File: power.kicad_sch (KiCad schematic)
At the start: 24 parts, among them Q1 DMN3008SFG, Q2 DMN3008SFG, U1 AP33771, U2 AP62150WU

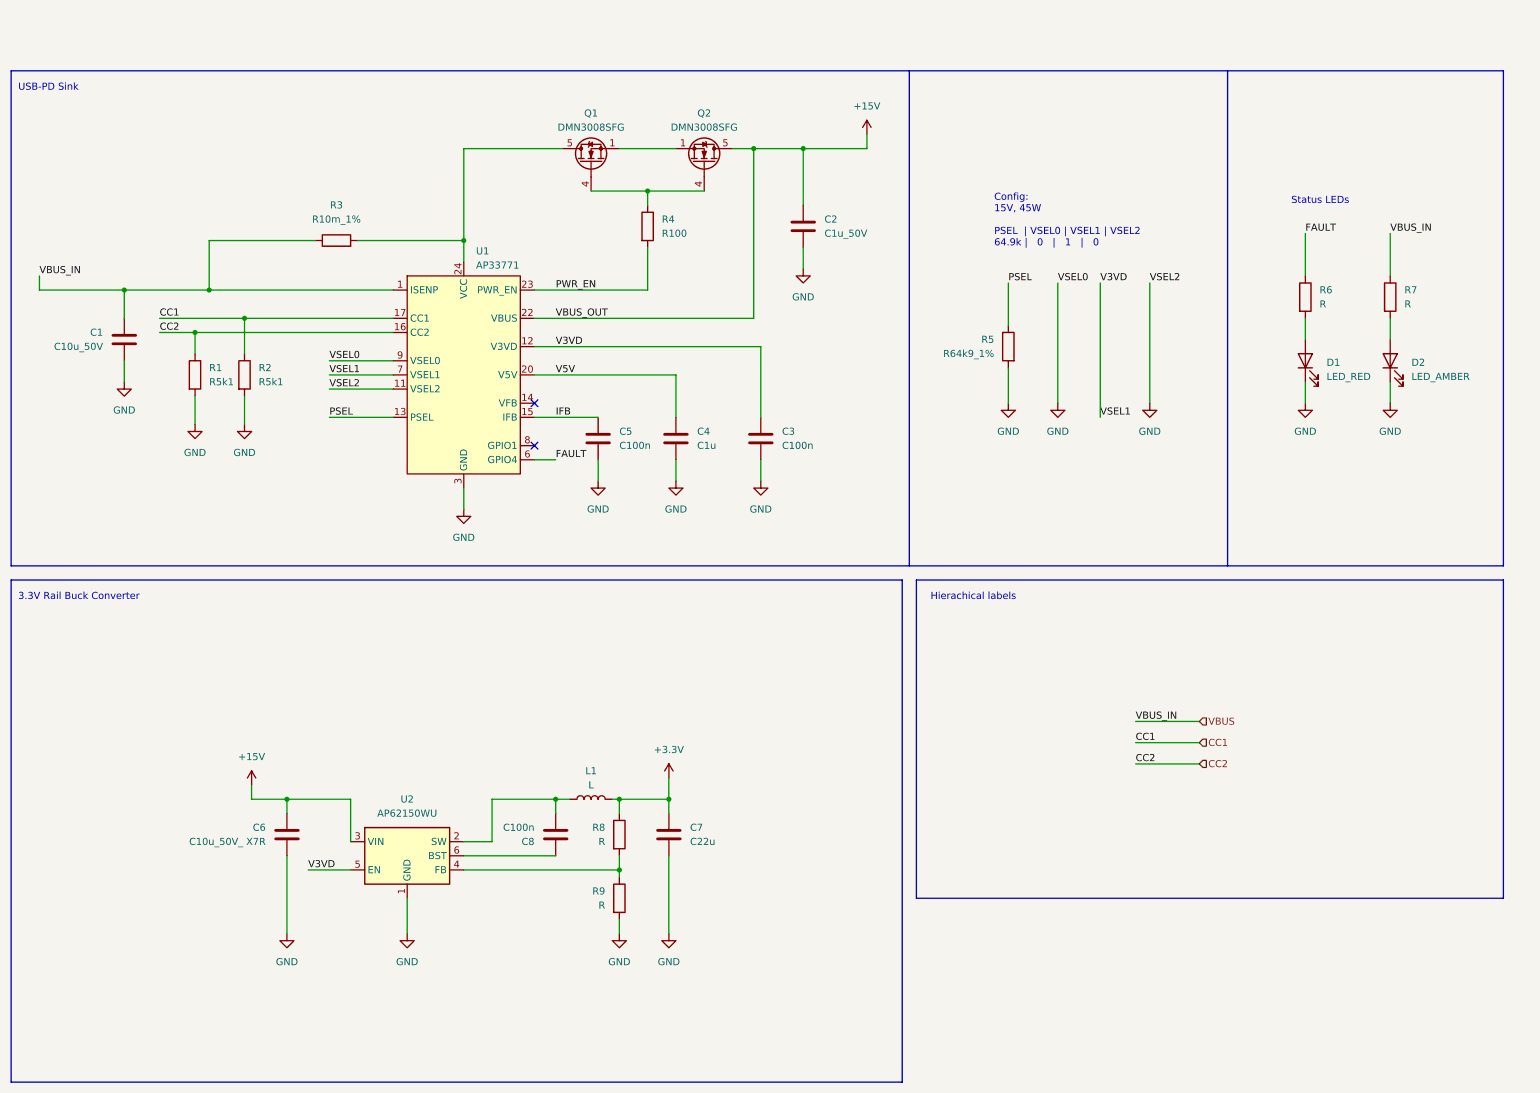
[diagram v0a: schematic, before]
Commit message: Add ESP32-S3-WROOM-1, 5V rail and UI sheet
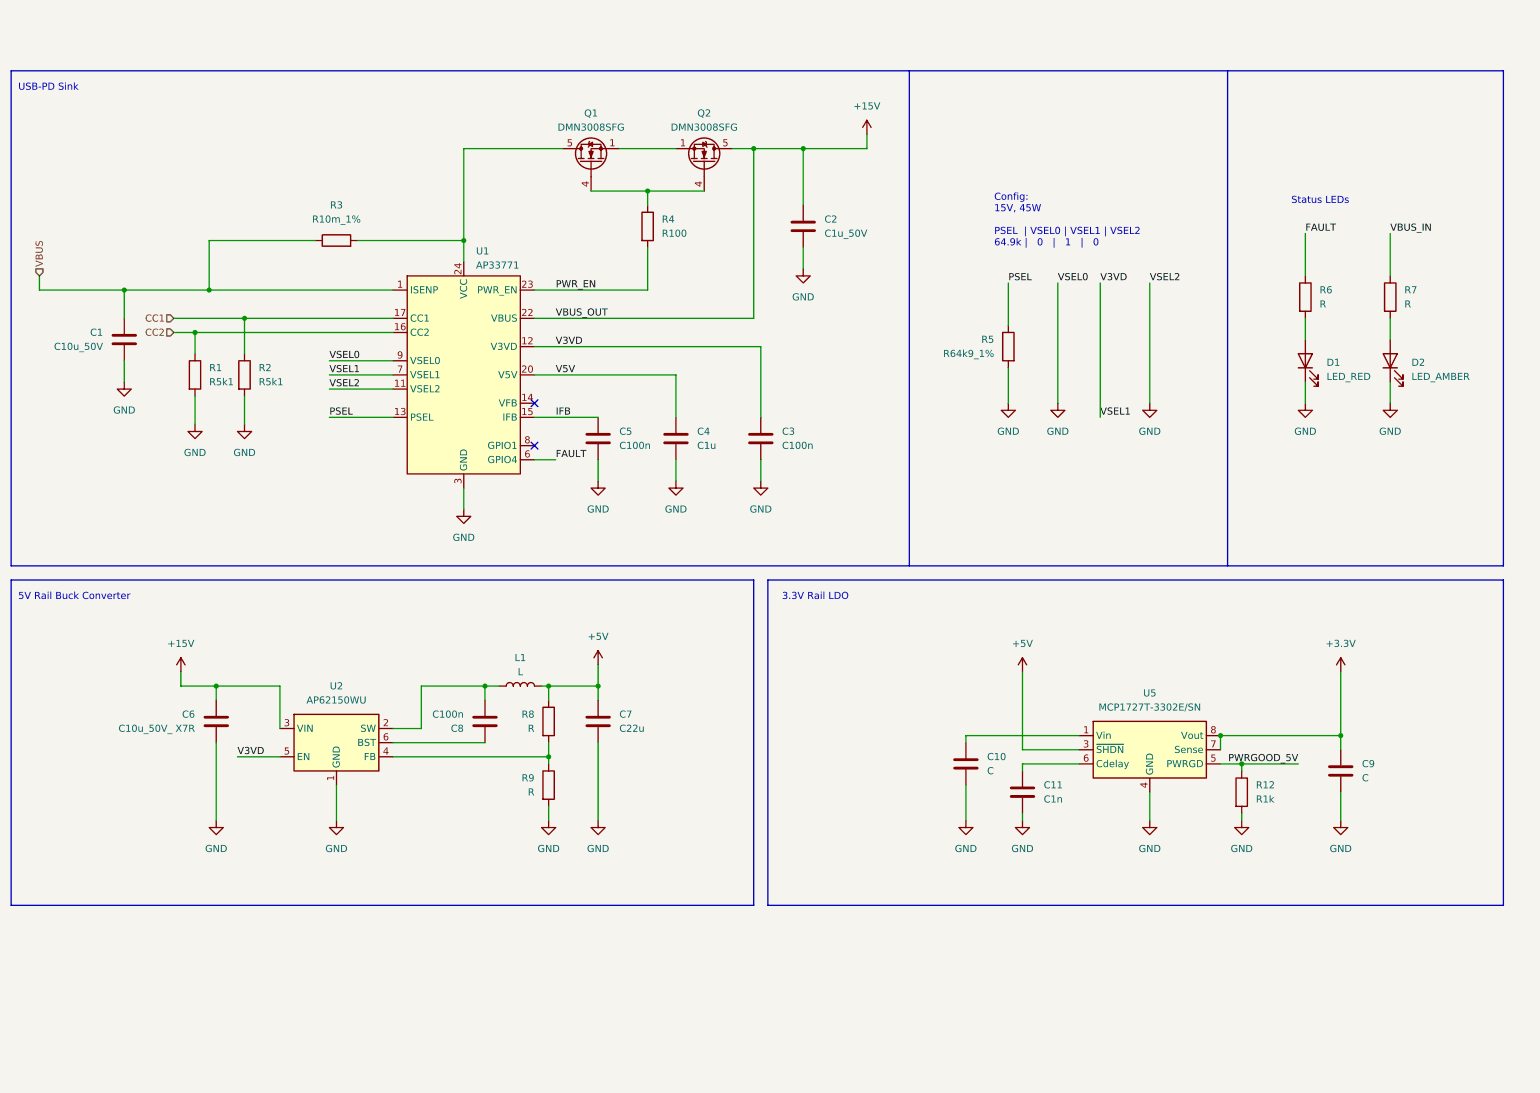
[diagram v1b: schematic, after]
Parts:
- added C10, C9: C, symbol Device:C
- added C11: C1n, symbol Device:C
- added R12: R1k, symbol Device:R
- added U5: MCP1727T-3302E/SN, Package_SO:SOIC-8_3.9x4.9mm_P1.27mm, symbol Regulator_Linear:MCP1727-3302xSN
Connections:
- net +3.3V: now also C9.1, U5.7 (Sense), U5.8 (Vout); no longer C7.1, L1.2, R8.1
- net GND: now also C10.2, C11.2, C9.2, R12.2, U5.4 (GND)
- net VBUS: no longer R7.1
- new net: C10.1, U5.1 (Vin), U5.2 (Vin)
- new net: C11.1, U5.6 (Cdelay)
- new net +5V: C7.1, L1.2, R8.1, U5.3 (~{SHDN})
- new net PWRGOOD_5V: R12.1, U5.5 (PWRGD)
- new net VBUS_IN: R7.1
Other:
- note added: "3.3V Rail LDO"
- note added: "5V Rail Buck Converter"
- note removed: "3.3V Rail Buck Converter"
- note removed: "Hierachical labels"
- moved on the sheet: C6, C7, C8, L1, R8, R9, U2

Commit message: Finish first design
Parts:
- removed R12: R1k, symbol Device:R
- removed U5: MCP1727T-3302E/SN, Package_SO:SOIC-8_3.9x4.9mm_P1.27mm, symbol Regulator_Linear:MCP1727-3302xSN
- added C20: C100u_20V, Capacitor_SMD:CP_Elec_6.3x5.9, symbol Device:C_Polarized
- added L2: L3u3, Inductor_SMD:L_Coilcraft_LPS4018, symbol Device:L
- added R29: R31k6_1%, Resistor_SMD:R_0805_2012Metric, symbol Device:R
- added R31: R10k_1%, Resistor_SMD:R_0805_2012Metric, symbol Device:R
- added TP18, TP19, TP20, TP21, TP22, TP25, TP26: TestPoint_Small, TestPoint:TestPoint_Pad_D1.5mm, symbol Connector:TestPoint_Small
- added U4: AP62150WU, Package_TO_SOT_SMD:TSOT-23-6, symbol Regulator_Switching:AP62150WU
- added U5: USBLC6-2SC6, Package_TO_SOT_SMD:SOT-23-6, symbol Power_Protection:USBLC6-2SC6
- C1: value C10u_50V -> C10u_25V; footprint (none) -> Capacitor_SMD:C_0603_1608Metric; Mouser Part Number (none) -> 81-GRM188R61E106KA3J
- C10: value C -> C100n; footprint (none) -> Capacitor_SMD:C_0603_1608Metric; Mouser Part Number (none) -> 80-C0603C104K3R7867
- C11: value C1n -> C22u; footprint (none) -> Capacitor_SMD:C_0805_2012Metric; Mouser Part Number (none) -> 187-CL21A226MQQNNNF
- C2: value C1u_50V -> C1u_25V; footprint (none) -> Capacitor_SMD:C_0603_1608Metric; Mouser Part Number (none) -> 963-TMK107B7105MA-T
- C3, C5, C8: footprint (none) -> Capacitor_SMD:C_0603_1608Metric; Mouser Part Number (none) -> 80-C0603C104K3R7867
- C4: value C1u -> C1u_25V; footprint (none) -> Capacitor_SMD:C_0603_1608Metric; Mouser Part Number (none) -> 963-TMK107B7105MA-T
- C6: value C10u_50V_ X7R -> C10u_25V; footprint (none) -> Capacitor_SMD:C_0603_1608Metric; Mouser Part Number (none) -> 81-GRM188R61E106KA3J
- C7: footprint (none) -> Capacitor_SMD:C_0805_2012Metric; Mouser Part Number (none) -> 187-CL21A226MQQNNNF
- C9: value C -> C10u_25V; footprint (none) -> Capacitor_SMD:C_0603_1608Metric; Mouser Part Number (none) -> 81-GRM188R61E106KA3J
- D1: value LED_RED -> LTST-C230CKT; footprint (none) -> project:LTST-C230; Mouser Part Number (none) -> 859-LTST-C230CKT
- D2: value LED_AMBER -> LTST-C230KGKT; footprint (none) -> project:LTST-C230; Mouser Part Number (none) -> 859-LTST-C230KGKT
- L1: value L -> L3u3; footprint (none) -> Inductor_SMD:L_Coilcraft_LPS4018; Mouser Part Number (none) -> 994-LPS4018-332MRC
- Q1, Q2: Mouser Part Number (none) -> 621-DMN3008SFG-7
- R1, R2: footprint (none) -> Resistor_SMD:R_0603_1608Metric; Mouser Part Number (none) -> 667-ERJ-3EKF5101V
- R3: value R10m_1% -> R10m_1%_0.5W; footprint (none) -> Resistor_SMD:R_1206_3216Metric; Mouser Part Number (none) -> 504-MFL1206R0100FS
- R4: footprint (none) -> Resistor_SMD:R_0603_1608Metric; Mouser Part Number (none) -> 279-CRG0603F100R
- R5: footprint (none) -> Resistor_SMD:R_0603_1608Metric; Mouser Part Number (none) -> 603-RC0603FR-0764K9P
- R6: value R -> R300; footprint (none) -> Resistor_SMD:R_0805_2012Metric; Mouser Part Number (none) -> 791-WR08X3000FTL
- R7: value R -> R2k7; footprint (none) -> Resistor_SMD:R_0805_2012Metric; Mouser Part Number (none) -> 279-CRGCQ0805F2K7
- R8: value R -> R52k3_1%; footprint (none) -> Resistor_SMD:R_0805_2012Metric; Mouser Part Number (none) -> 652-CR0805FX-5232ELF
- R9: value R -> R10k_1%; footprint (none) -> Resistor_SMD:R_0805_2012Metric; Mouser Part Number (none) -> 71-CRCW0805-10K-E3
- U1: Mouser Part Number (none) -> 621-AP33771DKZ-13
- U2: Mouser Part Number (none) -> 621-AP62150WU-7
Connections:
- net VBUS_IN is gone; now on net +15V: R7.1
- net +15V: now also C20.1, TP20.1
- net +3.3V: now also C11.1, U2.5 (EN), L2.2, R29.1, TP26.1; no longer C9.1
- net +5V: now also TP25.1
- net GND: now also C20.2, R31.2, U4.1 (GND), U5.2 (GND); no longer C10.2
- net V3VD: now also TP21.1, U4.5 (EN); no longer U2.5 (EN)
- net V5V: now also TP22.1, U5.5 (VBUS)
- net VBUS: now also TP18.1
- net 5V_BUCK_SW: now reaches C8.1, L1.1, U2.2 (SW)
- net 5V_BUCK_FB: now reaches R8.2, R9.1, U2.4 (FB)
- net PWR_EN_GATE: now reaches Q1.4 (G), Q2.4 (G), R4.1
- net 3V3_BUCK_SW: now reaches C10.1
- net 3V3_BUCK_SW: now also L2.1, U4.2 (SW)
- net 5V_BUCK_BST: now reaches C8.2, U2.6 (BST)
- net PWR_SOURCE_DRAIN: now reaches Q1.1 (S), Q1.2 (S), Q1.3 (S), Q2.1 (S), Q2.2 (S), Q2.3 (S)
- net PWR_VCC: now reaches Q1.5 (D), R3.2, U1.24 (VCC)
- net PWR_VCC: now also C9.1, TP19.1, U4.3 (VIN)
- net FAULT renamed PWR_FAULT
- new net 3V3_BUCK_BST: C10.2, U4.6 (BST)
- new net 3V3_BUCK_FB: R29.2, R31.1, U4.4 (FB)
- new net USB_D+: U5.1 (I/O1), U5.6 (I/O1)
- new net USB_D-: U5.3 (I/O2), U5.4 (I/O2)
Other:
- note added: "15V USB-PD Sink (60W/4A) supply for: - Valves - Main / Aux. Pump & Driver - 5V Buck Converter Decided to use 15V for Pumps and Valves, since the PD-Sink can't negotiate 12V. Also adding another 12V rail would raise the cost and complexity. Did some tests with the Pumps and Valves, they get a bit hotter than with 12V but since they are not driven too long this should not be a Problem."
- note added: "3.3V Rail Buck(4.95W/1.5A) supply for: - MCU - Display used recommended values from datasheet page 15, table 1"
- note added: "5V Rail Buck Converter (7.5W/1.5A) supply for: - Servo - HX711 used recommended values from datasheet page 15, table 1"
- note added: "Check: Find cheaper replacement"
- note added: "Config: 15V, | 60W | 15V | | PSEL | VSEL0 | VSEL1 | VSEL2 | | 75k | 0 | 1 | 0 | see datasheet page 2"
- note added: "MCU should be able to also run before 15V can be supplied reliably!! PWR_VCC can be either 5V or 15V"
- note added: "Shunt power rating: Voltage drop: 4A * 0.01R = 0.04V Power dissipation: 0.04V * 4A = 0.16W Safe power rating: 2 * 0.16W = 0.32W"
- note added: "Status LEDs If = 5mA Vf = 1.8V Vfault = 3.3V --> R=300 15V --> R=2k7"
- note added: "USB ESD Protection"
- note added: "green"
- note added: "red"
- note removed: "3.3V Rail LDO"
- note removed: "5V Rail Buck Converter"
- note removed: "Config: 15V, 45W PSEL | VSEL0 | VSEL1 | VSEL2 64.9k | 0 | 1 | 0"
- note removed: "Status LEDs"
- note removed: "USB-PD Sink"
- moved on the sheet: C1, C2, C3, C4, C5, C6, C7, C8, D1, D2, L1, Q1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

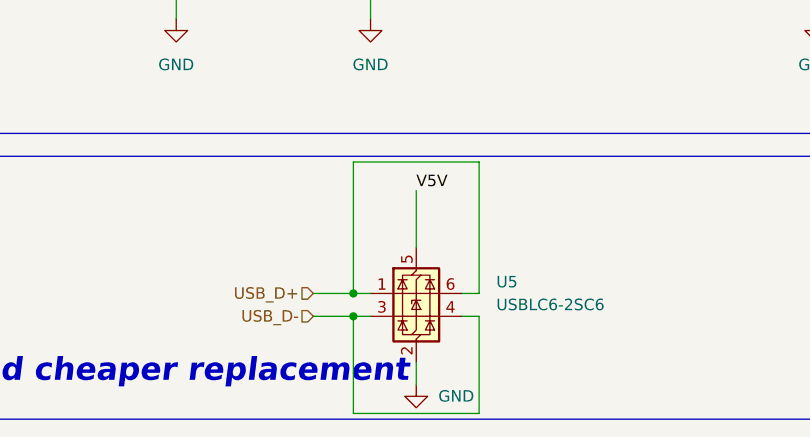
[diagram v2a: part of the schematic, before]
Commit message: Improve USB ESD connection
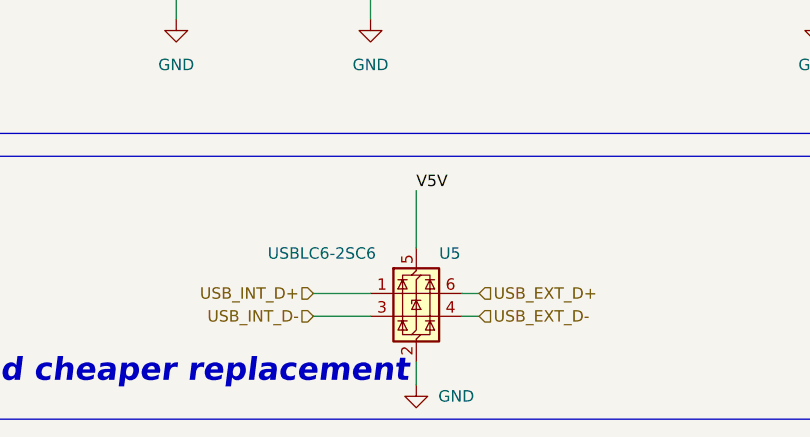
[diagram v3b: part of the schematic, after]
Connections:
- net USB_D+ renamed USB_EXT_D+
- net USB_EXT_D+: no longer U5.1 (I/O1)
- net USB_D- renamed USB_EXT_D-
- net USB_EXT_D-: no longer U5.3 (I/O2)
- new net USB_INT_D+: U5.1 (I/O1)
- new net USB_INT_D-: U5.3 (I/O2)
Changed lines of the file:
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@@
   (junction (at 55.88 60.96) (diameter 0) (color 0 0 0 0)
   )
-  (junction (at 76.2 184.15) (diameter 0) (color 0 0 0 0)
-  )
   (junction (at 132.08 127) (diameter 0) (color 0 0 0 0)
   )
@@
   )
   (junction (at 56.515 127) (diameter 0) (color 0 0 0 0)
-  )
-  (junction (at 76.2 181.61) (diameter 0) (color 0 0 0 0)
   )
   (junction (at 49.53 55.88) (diameter 0) (color 0 0 0 0)
@@
     (stroke (width 0) (type default))
   )
-  (wire (pts (xy 76.2 194.945) (xy 90.17 194.945))
-    (stroke (width 0) (type default))
-  )
   (wire (pts (xy 194.31 48.26) (xy 194.31 55.88))
     (stroke (width 0) (type default))
@@
     (stroke (width 0) (type default))
   )
-  (wire (pts (xy 76.2 184.15) (xy 76.2 194.945))
-    (stroke (width 0) (type default))
-  )
   (wire (pts (xy 127.635 139.7) (xy 127.635 140.97))
     (stroke (width 0) (type default))
@@
     (stroke (width 0) (type default))
   )
-  (wire (pts (xy 90.17 167.005) (xy 90.17 181.61))
-    (stroke (width 0) (type default))
-  )
   (wire (pts (xy 220.345 134.62) (xy 225.425 134.62))
     (stroke (width 0) (type default))
@@
     (stroke (width 0) (type default))
   )
-  (wire (pts (xy 76.2 184.15) (xy 78.105 184.15))
+  (wire (pts (xy 71.755 184.15) (xy 78.105 184.15))
     (stroke (width 0) (type default))
   )
@@
     (stroke (width 0) (type default))
   )
-  (wire (pts (xy 90.17 194.945) (xy 90.17 184.15))
-    (stroke (width 0) (type default))
-  )
   (wire (pts (xy 19.05 55.88) (xy 27.94 55.88))
     (stroke (width 0) (type default))
@@
     (stroke (width 0) (type default))
   )
-  (wire (pts (xy 76.2 167.005) (xy 90.17 167.005))
-    (stroke (width 0) (type default))
-  )
   (wire (pts (xy 259.715 127) (xy 259.715 129.54))
     (stroke (width 0) (type default))
@@
     (stroke (width 0) (type default))
   )
-  (wire (pts (xy 76.2 181.61) (xy 78.105 181.61))
+  (wire (pts (xy 71.755 181.61) (xy 78.105 181.61))
     (stroke (width 0) (type default))
   )
@@
     (stroke (width 0) (type default))
   )
-  (wire (pts (xy 76.2 181.61) (xy 76.2 167.005))
-    (stroke (width 0) (type default))
-  )
   (wire (pts (xy 259.715 137.16) (xy 259.715 139.7))
     (stroke (width 0) (type default))
@@
     (stroke (width 0) (type default))
   )
-  (wire (pts (xy 71.755 181.61) (xy 76.2 181.61))
-    (stroke (width 0) (type default))
-  )
   (wire (pts (xy 147.32 30.48) (xy 151.765 30.48))
     (stroke (width 0) (type default))
   )
   (wire (pts (xy 268.605 123.19) (xy 268.605 127))
-    (stroke (width 0) (type default))
-  )
-  (wire (pts (xy 71.755 184.15) (xy 76.2 184.15))
     (stroke (width 0) (type default))
   )
@@
     (effects (font (size 1.27 1.27)) (justify right))
   )
-  (hierarchical_label "USB_D+" (shape input) (at 71.755 181.61 180) (fields_autoplaced)
-    (effects (font (size 1.27 1.27)) (justify right))
+  (hierarchical_label "USB_EXT_D+" (shape input) (at 90.17 181.61 0) (fields_autoplaced)
+    (effects (font (size 1.27 1.27)) (justify left))
   )
   (hierarchical_label "VBUS" (shape input) (at 19.05 53.34 0) (fields_autoplaced)
     (effects (font (size 1.27 1.27)) (justify left))
   )
+  (hierarchical_label "USB_INT_D-" (shape input) (at 71.755 184.15 180) (fields_autoplaced)
+    (effects (font (size 1.27 1.27)) (justify right))
+  )
   (hierarchical_label "CC1" (shape input) (at 43.18 60.96 180) (fields_autoplaced)
     (effects (font (size 1.27 1.27)) (justify right))
   )
-  (hierarchical_label "USB_D-" (shape input) (at 71.755 184.15 180) (fields_autoplaced)
+  (hierarchical_label "USB_INT_D+" (shape input) (at 71.755 181.61 180) (fields_autoplaced)
     (effects (font (size 1.27 1.27)) (justify right))
+  )
+  (hierarchical_label "USB_EXT_D-" (shape input) (at 90.17 184.15 0) (fields_autoplaced)
+    (effects (font (size 1.27 1.27)) (justify left))
   )
   (symbol (lib_id "Device:L") (at 122.555 127 90) (unit 1)
@@
   (symbol (lib_id "Power_Protection:USBLC6-2SC6") (at 83.185 181.61 0) (unit 1)
     (in_bom yes) (on_board yes) (dnp no)
-    (property "Reference" "U5" (at 92.075 180.34 0)
-      (effects (font (size 1.27 1.27)) (justify left))
-    )
-    (property "Value" "USBLC6-2SC6" (at 92.075 182.88 0)
-      (effects (font (size 1.27 1.27)) (justify left))
-    )
+    (property "Reference" "U5" (at 85.725 177.165 0)
+      (effects (font (size 1.27 1.27)) (justify left))
+    )
+    (property "Value" "USBLC6-2SC6" (at 66.675 177.165 0)
+      (effects (font (size 1.27 1.27)) (justify left))
+    )
